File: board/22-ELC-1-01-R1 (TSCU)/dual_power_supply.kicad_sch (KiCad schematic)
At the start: 12 parts, among them U1 TPS5430DDA

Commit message: Ready for review
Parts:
- renumbered C4 to C13, C5 to C14, C2 to C15, C3 to C16, C31 to C17, C32 to C18, C33 to C19, D6 to D10, R4 to R31, R5 to R32, U1 to U6
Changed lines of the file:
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@@
   (symbol (lib_id "Regulator_Switching:TPS5430DDA") (at 124.46 130.81 0) (unit 1)
     (in_bom yes) (on_board yes)
-    (property "Reference" "U1" (id 0) (at 124.46 118.9482 0))
+    (property "Reference" "U6" (id 0) (at 124.46 118.9482 0))
     (property "Value" "TPS5430DDA" (id 1) (at 124.46 121.2596 0))
     (property "Footprint" "Package_SO:TI_SO-PowerPAD-8_ThermalVias" (id 2) (at 125.73 139.7 0)
@@
   (symbol (lib_id "power:GND") (at 123.19 144.78 0) (unit 1)
     (in_bom yes) (on_board yes)
-    (property "Reference" "#PWR020" (id 0) (at 123.19 151.13 0)
+    (property "Reference" "#PWR069" (id 0) (at 123.19 151.13 0)
       (effects (font (size 1.27 1.27)) hide)
     )
@@
   (symbol (lib_id "Device:C_Small") (at 143.51 125.73 270) (mirror x) (unit 1)
     (in_bom yes) (on_board yes)
-    (property "Reference" "C3" (id 0) (at 144.78 120.65 90)
+    (property "Reference" "C16" (id 0) (at 144.78 120.65 90)
       (effects (font (size 1.27 1.27)) (justify right))
     )
@@
   (symbol (lib_id "Device:D_Schottky") (at 156.21 129.54 270) (unit 1)
     (in_bom yes) (on_board yes)
-    (property "Reference" "D6" (id 0) (at 158.2166 128.3716 90)
+    (property "Reference" "D10" (id 0) (at 158.2166 128.3716 90)
       (effects (font (size 1.27 1.27)) (justify left))
     )
@@
   (symbol (lib_id "power:GND") (at 156.21 133.35 0) (unit 1)
     (in_bom yes) (on_board yes)
-    (property "Reference" "#PWR021" (id 0) (at 156.21 139.7 0)
+    (property "Reference" "#PWR070" (id 0) (at 156.21 139.7 0)
       (effects (font (size 1.27 1.27)) hide)
     )
@@
   (symbol (lib_id "power:GND") (at 182.88 130.81 0) (unit 1)
     (in_bom yes) (on_board yes)
-    (property "Reference" "#PWR024" (id 0) (at 182.88 137.16 0)
+    (property "Reference" "#PWR071" (id 0) (at 182.88 137.16 0)
       (effects (font (size 1.27 1.27)) hide)
     )
@@
   (symbol (lib_id "Device:R") (at 213.36 133.35 0) (unit 1)
     (in_bom yes) (on_board yes)
-    (property "Reference" "R4" (id 0) (at 215.138 132.1816 0)
+    (property "Reference" "R31" (id 0) (at 215.138 132.1816 0)
       (effects (font (size 1.27 1.27)) (justify left))
     )
@@
   (symbol (lib_id "Device:R") (at 213.36 148.59 0) (unit 1)
     (in_bom yes) (on_board yes)
-    (property "Reference" "R5" (id 0) (at 215.138 147.4216 0)
+    (property "Reference" "R32" (id 0) (at 215.138 147.4216 0)
       (effects (font (size 1.27 1.27)) (justify left))
     )
@@
   (symbol (lib_id "power:GND") (at 213.36 152.4 0) (unit 1)
     (in_bom yes) (on_board yes)
-    (property "Reference" "#PWR025" (id 0) (at 213.36 158.75 0)
+    (property "Reference" "#PWR074" (id 0) (at 213.36 158.75 0)
       (effects (font (size 1.27 1.27)) hide)
     )
@@
   (symbol (lib_id "Device:C_Small") (at 100.33 130.81 0) (mirror x) (unit 1)
     (in_bom yes) (on_board yes)
-    (property "Reference" "C2" (id 0) (at 105.41 132.08 90)
+    (property "Reference" "C15" (id 0) (at 105.41 132.08 90)
       (effects (font (size 1.27 1.27)) (justify right))
     )
@@
   (symbol (lib_id "power:GND") (at 100.33 133.35 0) (unit 1)
     (in_bom yes) (on_board yes)
-    (property "Reference" "#PWR019" (id 0) (at 100.33 139.7 0)
+    (property "Reference" "#PWR068" (id 0) (at 100.33 139.7 0)
       (effects (font (size 1.27 1.27)) hide)
     )
@@
   (symbol (lib_id "Device:C_Small") (at 90.17 130.81 0) (mirror x) (unit 1)
     (in_bom yes) (on_board yes)
-    (property "Reference" "C5" (id 0) (at 95.25 132.08 90)
+    (property "Reference" "C14" (id 0) (at 95.25 132.08 90)
       (effects (font (size 1.27 1.27)) (justify right))
     )
@@
   (symbol (lib_id "Device:C_Small") (at 78.74 130.81 0) (mirror x) (unit 1)
     (in_bom yes) (on_board yes)
-    (property "Reference" "C4" (id 0) (at 83.82 132.08 90)
+    (property "Reference" "C13" (id 0) (at 83.82 132.08 90)
       (effects (font (size 1.27 1.27)) (justify right))
     )
@@
   (symbol (lib_id "power:GND") (at 90.17 133.35 0) (unit 1)
     (in_bom yes) (on_board yes)
-    (property "Reference" "#PWR023" (id 0) (at 90.17 139.7 0)
+    (property "Reference" "#PWR067" (id 0) (at 90.17 139.7 0)
       (effects (font (size 1.27 1.27)) hide)
     )
@@
   (symbol (lib_id "power:GND") (at 78.74 133.35 0) (unit 1)
     (in_bom yes) (on_board yes)
-    (property "Reference" "#PWR022" (id 0) (at 78.74 139.7 0)
+    (property "Reference" "#PWR066" (id 0) (at 78.74 139.7 0)
       (effects (font (size 1.27 1.27)) hide)
     )
@@
   (symbol (lib_id "Device:C_Small") (at 182.88 128.27 0) (mirror x) (unit 1)
     (in_bom yes) (on_board yes)
-    (property "Reference" "C31" (id 0) (at 187.96 129.54 90)
+    (property "Reference" "C17" (id 0) (at 187.96 129.54 90)
       (effects (font (size 1.27 1.27)) (justify right))
     )
@@
   (symbol (lib_id "Device:C_Small") (at 191.77 128.27 0) (mirror x) (unit 1)
     (in_bom yes) (on_board yes)
-    (property "Reference" "C32" (id 0) (at 196.85 129.54 90)
+    (property "Reference" "C18" (id 0) (at 196.85 129.54 90)
       (effects (font (size 1.27 1.27)) (justify right))
     )
@@
   (symbol (lib_id "power:GND") (at 191.77 130.81 0) (unit 1)
     (in_bom yes) (on_board yes)
-    (property "Reference" "#PWR033" (id 0) (at 191.77 137.16 0)
+    (property "Reference" "#PWR072" (id 0) (at 191.77 137.16 0)
       (effects (font (size 1.27 1.27)) hide)
     )
@@
   (symbol (lib_id "Device:C_Small") (at 200.66 128.27 0) (mirror x) (unit 1)
     (in_bom yes) (on_board yes)
-    (property "Reference" "C33" (id 0) (at 205.74 129.54 90)
+    (property "Reference" "C19" (id 0) (at 205.74 129.54 90)
       (effects (font (size 1.27 1.27)) (justify right))
     )
@@
   (symbol (lib_id "power:GND") (at 200.66 130.81 0) (unit 1)
     (in_bom yes) (on_board yes)
-    (property "Reference" "#PWR042" (id 0) (at 200.66 137.16 0)
-      (effects (font (size 1.27 1.27)) hide)
-    )
+    (property "Reference" "#PWR073" (id 0) (at 200.66 137.16 0)
+      (effects (font (size 1.27 1.27)) hide)
+    )

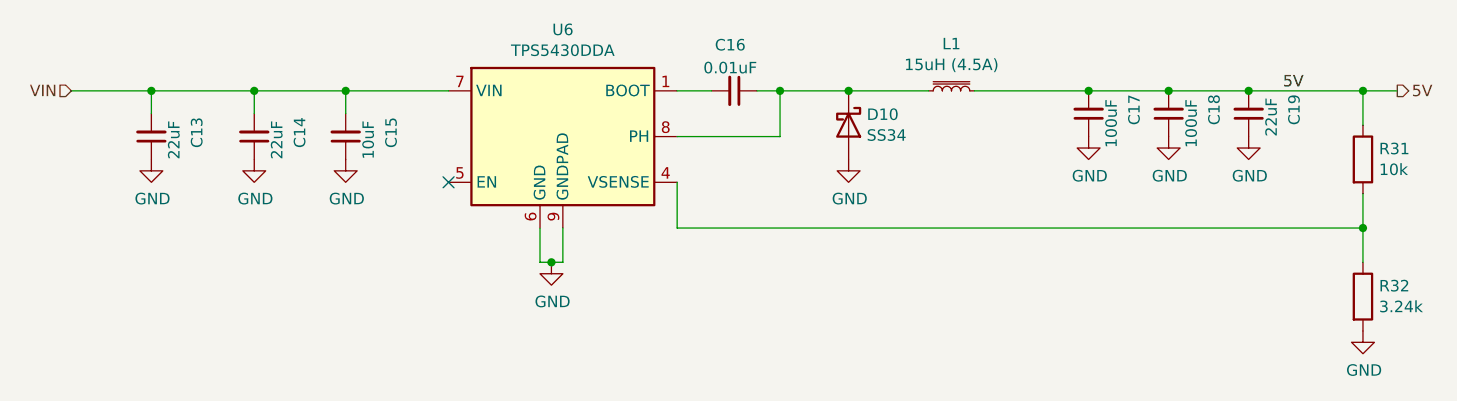
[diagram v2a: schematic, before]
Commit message: All good except need to switch everything to accepting 24v power
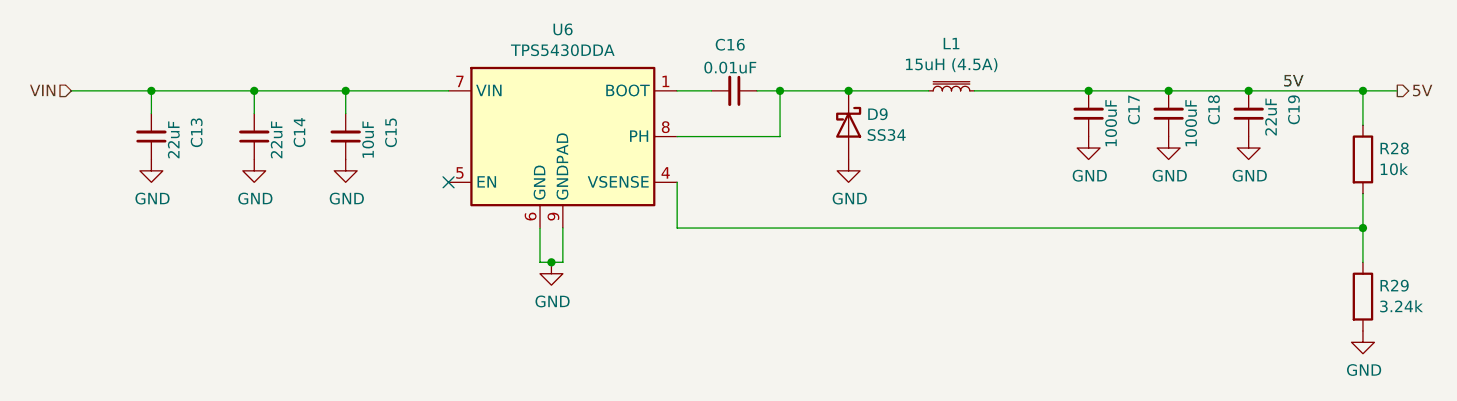
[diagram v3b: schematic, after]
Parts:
- renumbered D10 to D9, R31 to R28, R32 to R29
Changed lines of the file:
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@@
   (symbol (lib_id "Device:D_Schottky") (at 156.21 129.54 270) (unit 1)
     (in_bom yes) (on_board yes)
-    (property "Reference" "D10" (id 0) (at 158.2166 128.3716 90)
+    (property "Reference" "D9" (id 0) (at 158.2166 128.3716 90)
       (effects (font (size 1.27 1.27)) (justify left))
     )
@@
   (symbol (lib_id "Device:R") (at 213.36 133.35 0) (unit 1)
     (in_bom yes) (on_board yes)
-    (property "Reference" "R31" (id 0) (at 215.138 132.1816 0)
+    (property "Reference" "R28" (id 0) (at 215.138 132.1816 0)
       (effects (font (size 1.27 1.27)) (justify left))
     )
@@
   (symbol (lib_id "Device:R") (at 213.36 148.59 0) (unit 1)
     (in_bom yes) (on_board yes)
-    (property "Reference" "R32" (id 0) (at 215.138 147.4216 0)
+    (property "Reference" "R29" (id 0) (at 215.138 147.4216 0)
       (effects (font (size 1.27 1.27)) (justify left))
     )
